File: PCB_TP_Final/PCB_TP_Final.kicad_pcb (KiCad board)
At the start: 2 copper layers, 71 x 135 mm, 21 parts, among them CN10 Conn_02x17_Odd_Even, CN7 Conn_02x10_Odd_Even, CN8 Conn_02x08_Odd_Even, CN9 Conn_02x15_Odd_Even, J1 Conn_01x09, M1 POWER_MB_V2, SW1 SW_Push, U1 NODEMCU_ESP12

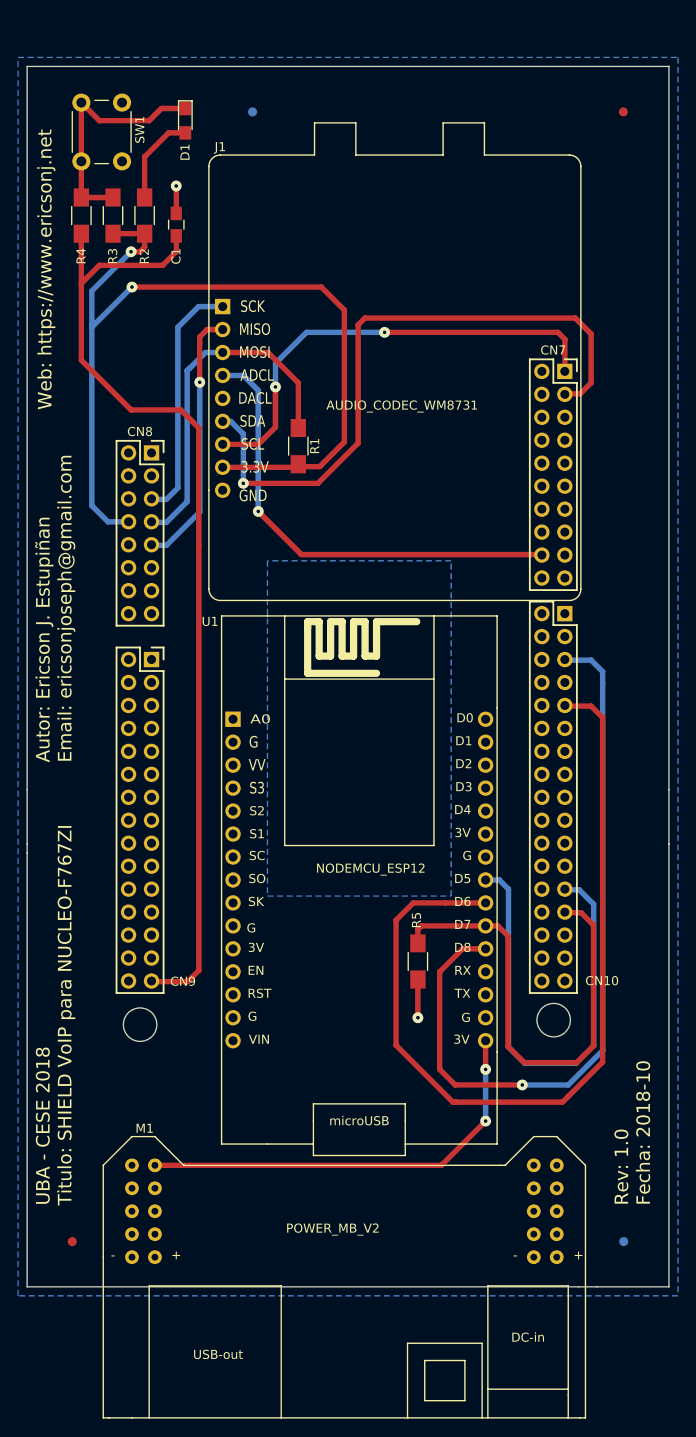
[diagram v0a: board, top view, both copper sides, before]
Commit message: Add changes in via size and power track size
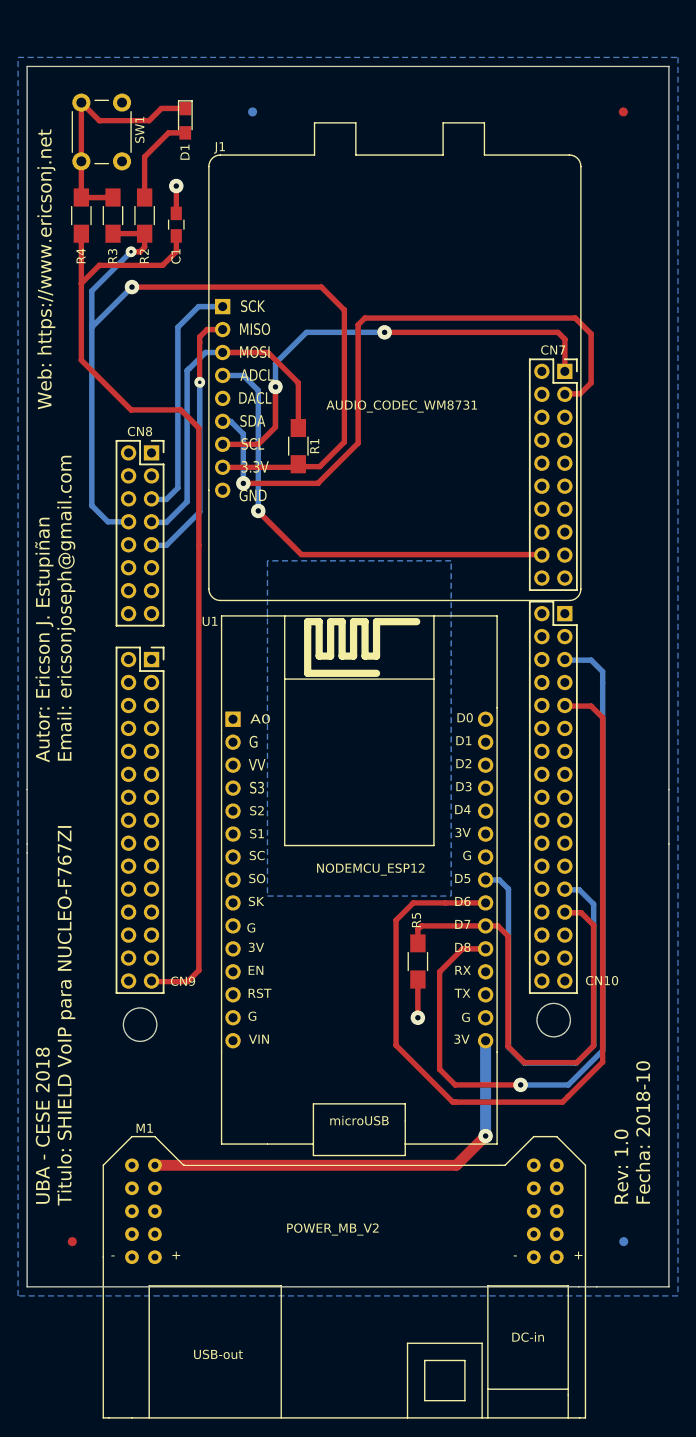
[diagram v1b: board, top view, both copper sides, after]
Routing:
- net +3V3: track 47.5 -> 48.5 mm, vias 2 -> 1
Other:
- net class Default: via_dia 1.2 -> 1.6; via_drill 0.4 -> 0.6
